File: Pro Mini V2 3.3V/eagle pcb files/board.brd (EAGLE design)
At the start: 39 x 39 mm, 4 parts, among them X1 B8B-PH-KL

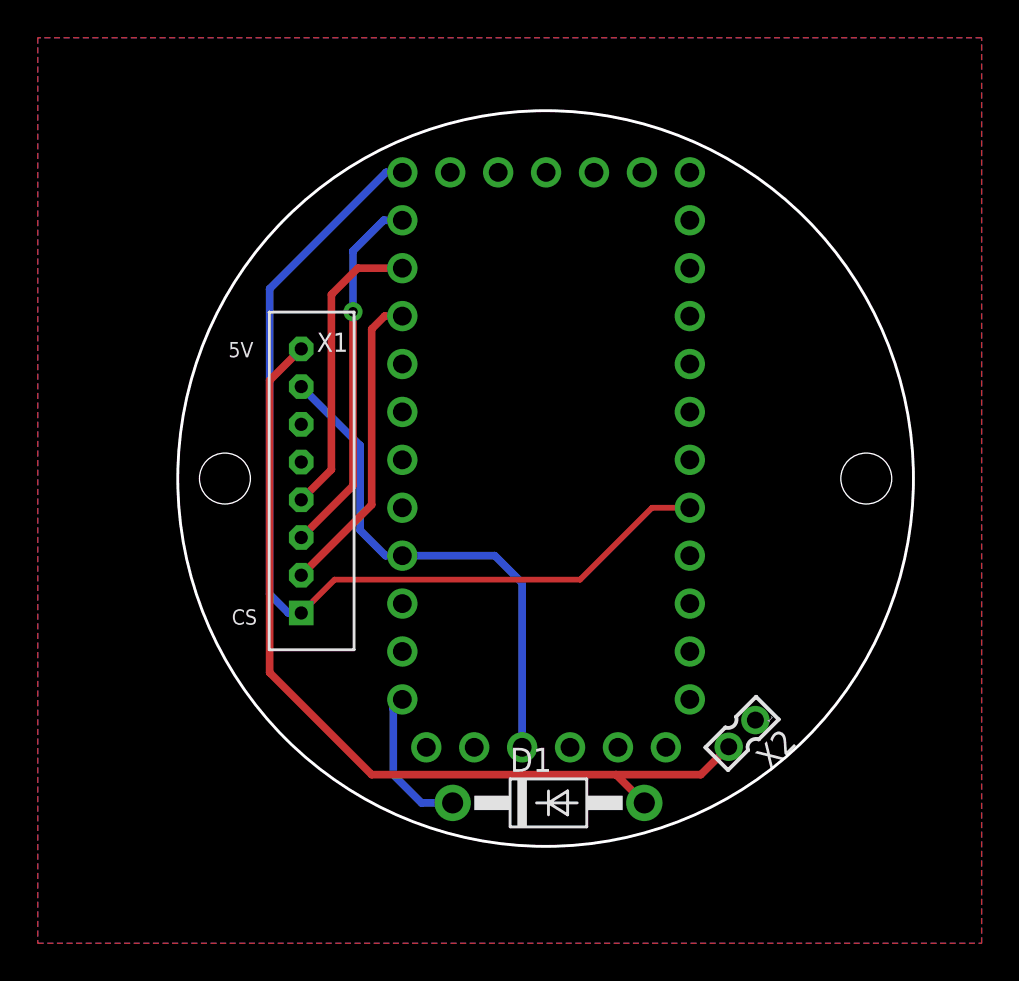
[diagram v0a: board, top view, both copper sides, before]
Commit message: #9 Update readme and PCB files
- add wheelbase damage warning
- add note to uncomment lines
- remove connection of 5V to RAW (including diode)
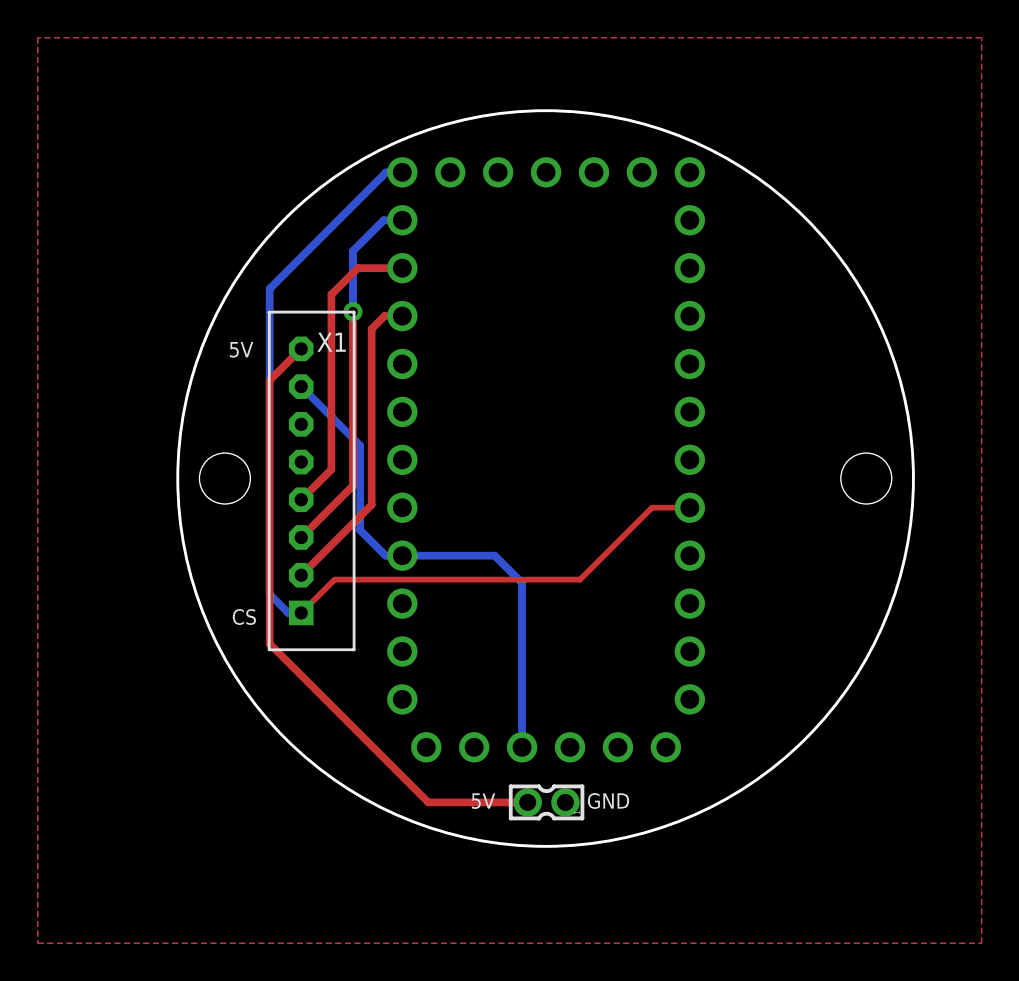
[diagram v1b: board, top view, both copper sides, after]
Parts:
- removed D1: 1N4004, adafruit:DO41-10
- moved X2 11.0 mm to (0.05, -17.2), turned to 90 degrees
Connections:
- net 4_5V: no longer D1.A
- net RAW: no longer D1.C
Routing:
- net 4_5V: track 47.2 -> 33.5 mm
- net RAW: track 7.96 -> 0.00 mm
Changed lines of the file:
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@@
 <drawing>
 <settings>
-<setting alwaysvectorfont="yes"/>
+<setting alwaysvectorfont="no"/>
 <setting verticaltext="up"/>
 </settings>
@@
 </layers>
 <board>
-<fusionsync huburn="a.cGVyc29uYWw6dWUyZDNmMGU2" projecturn="a.cGVyc29uYWw6dWUyZDNmMGU2IzIwMjAwMjE2MjY2MTc3MzUx" f3durn="urn:adsk.wipprod:dm.lineage:n3kzW-DEQbq8_7y4DWoqgQ" pcbguid="" lastpulledtime="" lastsyncedchangeguid="" latestrevisionid="26ae5165-9002-451a-95df-174b9d77579b" lastsyncedrevisionid="26ae5165-9002-451a-95df-174b9d77579b" lastboardhashguid="82892f39-adaf-334c-56e9-445799ba8b56" lastpushedtime="2020-09-23T17:38:56Z" linktopcb3d="true"/>
+<fusionsync huburn="a.cGVyc29uYWw6dWUyZDNmMGU2" projecturn="a.cGVyc29uYWw6dWUyZDNmMGU2IzIwMjAwMjE2MjY2MTc3MzUx" f3durn="urn:adsk.wipprod:dm.lineage:n3kzW-DEQbq8_7y4DWoqgQ" pcbguid="" lastpulledtime="" lastsyncedchangeguid="" latestrevisionid="26ae5165-9002-451a-95df-174b9d77579b" lastsyncedrevisionid="26ae5165-9002-451a-95df-174b9d77579b" lastboardhashguid="82892f39-adaf-334c-56e9-445799ba8b56" lastpushedtime="2020-09-23T17:38:56Z" linktopcb3d="false"/>
 <plain>
 <circle x="0" y="0" radius="19.5" width="0.1524" layer="20"/>
@@
 <text x="-16.8148" y="6.4262" size="0.8128" layer="21">5V</text>
 <text x="-16.637" y="-7.747" size="0.8128" layer="21">CS</text>
-<text x="9.271" y="-16.129" size="0.8128" layer="22" rot="MR0">5V</text>
-<text x="12.2428" y="-11.7094" size="0.8128" layer="22" rot="MR0">GND</text>
+<text x="-2.3876" y="-17.5006" size="0.8128" layer="22" rot="MR0">5V</text>
+<text x="4.699" y="-17.5006" size="0.8128" layer="22" rot="MR0">GND</text>
+<text x="2.1844" y="-17.5006" size="0.8128" layer="21">GND</text>
+<text x="-3.9878" y="-17.5006" size="0.8128" layer="21">5V</text>
 </plain>
 <attributes>
@@
 <elements>
 <element name="U$7" library="Arduino-clone" package="PRO-MINI-5BOT" override_package3d_urn="urn:adsk.eagle:package:23456791/2" override_package_urn="urn:adsk.eagle:footprint:23456792/1" value="PRO-MINI_5BOT" x="1.2954" y="14.9606" smashed="yes" rot="R180"/>
-<element name="D1" library="adafruit" library_urn="urn:adsk.eagle:library:420" package="DO41-10" package3d_urn="urn:adsk.eagle:package:6240344/1" override_package3d_urn="urn:adsk.eagle:package:23456826/2" override_package_urn="urn:adsk.eagle:footprint:6239679/1" value="1N4004" x="0.1524" y="-17.1958" smashed="yes">
-<attribute name="NAME" x="-1.8796" y="-15.5448" size="1.27" layer="25" ratio="10"/>
-<attribute name="VALUE" x="-1.8796" y="-19.9898" size="1.27" layer="27" ratio="10"/>
-</element>
 <element name="X1" library="con-JST PH" package="B8B-PH-K-S" value="B8B-PH-KL" x="-12.954" y="-0.127" smashed="yes" rot="R270">
 <attribute name="NAME" x="-11.303" y="7.732" size="1.016" layer="25" rot="R180" align="bottom-center"/>
 <attribute name="VALUE" x="-11.684" y="-7.127" size="1.016" layer="27" rot="R270" align="bottom-right"/>
 </element>
-<element name="X2" library="con-molex" library_urn="urn:adsk.eagle:library:165" package="87758-0216" package3d_urn="urn:adsk.eagle:package:8078894/1" value="" x="10.414" y="-13.5128" smashed="yes" rot="R135">
-<attribute name="MF" value="MOLEX" x="10.414" y="-13.5128" size="1.778" layer="27" rot="R135" display="off"/>
-<attribute name="MPN" value="87758-0216" x="10.414" y="-13.5128" size="1.778" layer="27" rot="R135" display="off"/>
-<attribute name="NAME" x="12.486809375" y="-13.16419375" size="1.27" layer="25" rot="R225"/>
-<attribute name="OC_FARNELL" value="unknown" x="10.414" y="-13.5128" size="1.778" layer="27" rot="R135" display="off"/>
-<attribute name="OC_NEWARK" value="94M1513" x="10.414" y="-13.5128" size="1.778" layer="27" rot="R135" display="off"/>
-<attribute name="POPULARITY" value="4" x="10.414" y="-13.5128" size="1.778" layer="27" rot="R135" display="off"/>
-<attribute name="VALUE" x="16.36628125" y="-11.871034375" size="1.27" layer="27" rot="R225"/>
+<element name="X2" library="con-molex" library_urn="urn:adsk.eagle:library:165" package="87758-0216" package3d_urn="urn:adsk.eagle:package:8078894/1" value="" x="0.0508" y="-17.1704" smashed="yes" rot="R90">
+<attribute name="MF" value="MOLEX" x="0.0508" y="-17.1704" size="1.778" layer="27" rot="R90" display="off"/>
+<attribute name="MPN" value="87758-0216" x="0.0508" y="-17.1704" size="1.778" layer="27" rot="R90" display="off"/>
+<attribute name="OC_FARNELL" value="unknown" x="0.0508" y="-17.1704" size="1.778" layer="27" rot="R90" display="off"/>
+<attribute name="OC_NEWARK" value="94M1513" x="0.0508" y="-17.1704" size="1.778" layer="27" rot="R90" display="off"/>
+<attribute name="POPULARITY" value="4" x="0.0508" y="-17.1704" size="1.778" layer="27" rot="R90" display="off"/>
+<attribute name="VALUE" x="5.420603125" y="-20.2184" size="1.27" layer="27" rot="R180"/>
 </element>
 </elements>
@@
 </signal>
 <signal name="4_5V">
-<contactref element="D1" pad="A"/>
 <contactref element="X1" pad="8"/>
 <wire x1="-12.954" y1="6.873" x2="-14.6304" y2="5.1966" width="0.4064" layer="1"/>
-<wire x1="-14.6304" y1="5.1966" x2="-14.6304" y2="-10.287" width="0.4064" layer="1"/>
-<wire x1="-14.6304" y1="-10.287" x2="-9.2202" y2="-15.6972" width="0.4064" layer="1"/>
-<wire x1="5.2324" y1="-17.1958" x2="3.7338" y2="-15.6972" width="0.4064" layer="1"/>
-<wire x1="-9.2202" y1="-15.6972" x2="3.7338" y2="-15.6972" width="0.4064" layer="1"/>
+<wire x1="-14.6304" y1="5.1966" x2="-14.6304" y2="-8.763" width="0.4064" layer="1"/>
 <contactref element="X2" pad="2"/>
-<wire x1="8.229596875" y1="-15.6972" x2="9.706890625" y2="-14.21990625" width="0.4064" layer="1"/>
-<wire x1="3.7338" y1="-15.6972" x2="8.229596875" y2="-15.6972" width="0.4064" layer="1"/>
+<wire x1="-6.223" y1="-17.1704" x2="-0.9492" y2="-17.1704" width="0.4064" layer="1"/>
+<wire x1="-14.6304" y1="-8.763" x2="-6.223" y2="-17.1704" width="0.4064" layer="1"/>
 </signal>
 <signal name="RAW">
-<contactref element="D1" pad="C"/>
 <contactref element="U$7" pad="RAW"/>
-<wire x1="-4.9276" y1="-17.1958" x2="-6.5786" y2="-17.1958" width="0.4064" layer="16"/>
-<wire x1="-6.5786" y1="-17.1958" x2="-8.0772" y2="-15.6972" width="0.4064" layer="16"/>
-<wire x1="-8.0772" y1="-15.6972" x2="-8.0772" y2="-12.192" width="0.4064" layer="16"/>
-<wire x1="-8.0772" y1="-12.192" x2="-7.5946" y2="-11.7094" width="0.4064" layer="16"/>
 </signal>
 </signals>
